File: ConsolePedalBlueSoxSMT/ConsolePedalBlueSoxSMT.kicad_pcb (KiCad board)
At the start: 2 copper layers, 100 x 60 mm, 53 parts, among them IC1 CD4013BE, J1 Conn_02x25_Counter_Clockwise, Q1 2N3904, Q2 2N3904, Q3 2N3904, U1 RC4558

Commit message: Minor changes
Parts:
- moved C100 76.4 mm to (174.2, 79.8), turned to 270 degrees
- moved C4 65.5 mm to (104.6, 81.8), turned to 270 degrees
- moved C101 58.9 mm to (160.0, 105.2), turned to 270 degrees
- moved C8 55.1 mm to (124.5, 96.0), turned to 90 degrees
- moved R102 51.2 mm to (135.2, 89.9), turned to 180 degrees
- moved C9 49.1 mm to (120.9, 96.0)
- moved R16 46.7 mm to (124.5, 101.6), turned to 90 degrees
- moved C2 41.0 mm to (127.0, 85.3), turned to 90 degrees
- moved R5 40.4 mm to (115.2, 72.6), turned to 0 degrees
- moved C102 32.3 mm to (138.7, 104.1), turned to 270 degrees
- moved R6 29.5 mm to (132.8, 85.9), turned to 180 degrees
- moved R101 28.6 mm to (130.2, 89.9), turned to 180 degrees
- moved R9 21.0 mm to (106.2, 90.9), turned to 180 degrees
- moved R13 19.8 mm to (160.0, 96.3)
- moved R15 18.5 mm to (156.0, 96.3)
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
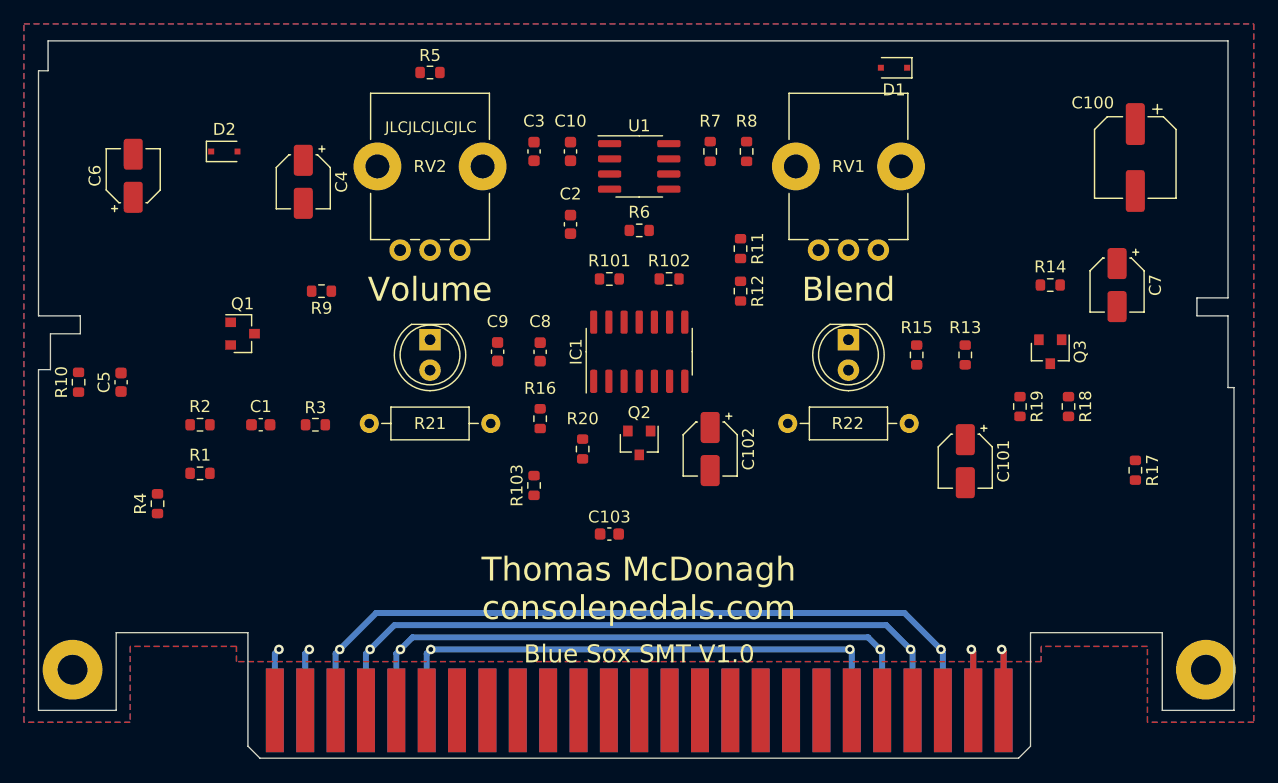
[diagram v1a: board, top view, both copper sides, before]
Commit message: Finished component placement
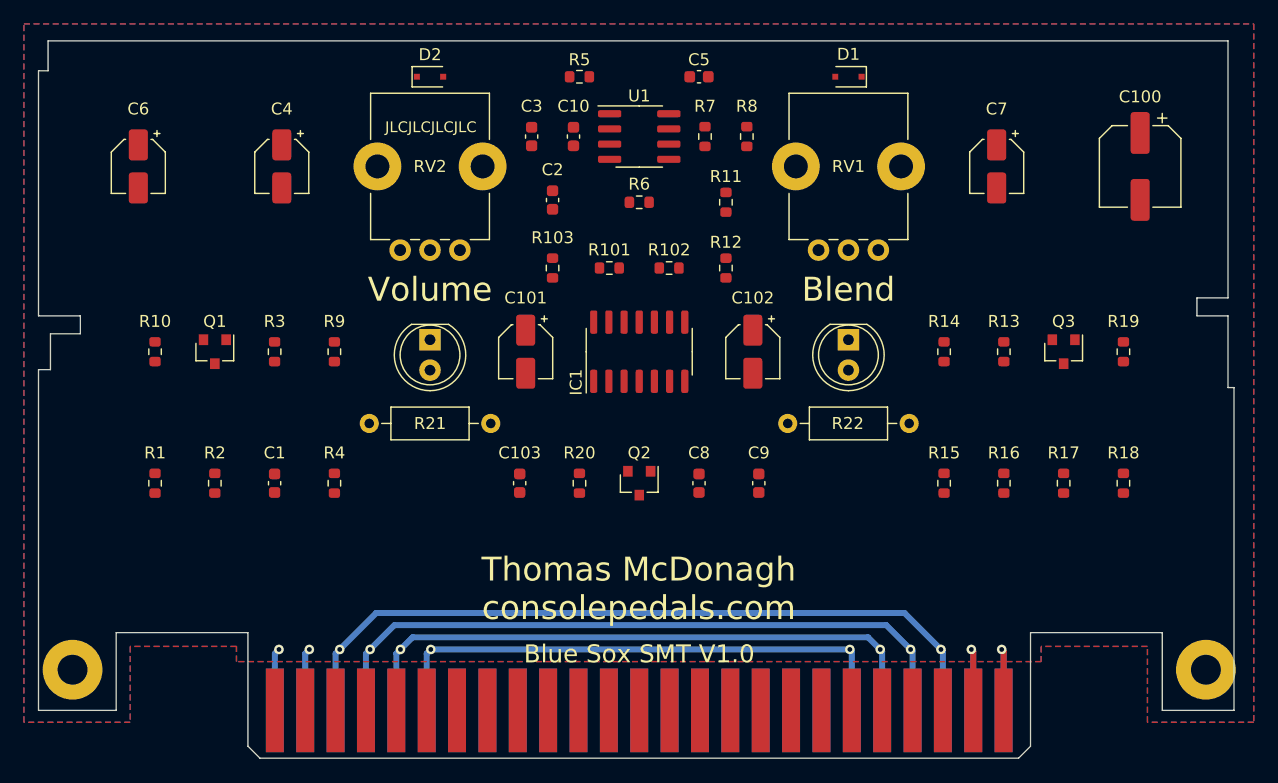
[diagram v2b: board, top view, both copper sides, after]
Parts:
- moved C5 54.7 mm to (137.8, 73.0), turned to 0 degrees
- moved R16 39.2 mm to (163.2, 107.0), turned to 270 degrees
- moved C101 37.9 mm to (123.2, 96.0)
- moved C9 24.5 mm to (142.8, 107.0)
- moved D2 18.3 mm to (115.2, 73.0)
- moved R103 18.3 mm to (125.5, 89.0)
- moved C8 17.2 mm to (137.8, 107.0)
- moved R4 14.9 mm to (107.2, 107.0), turned to 270 degrees
- moved C7 14.1 mm to (162.7, 80.5)
- moved R5 12.5 mm to (127.8, 73.0)
- moved R15 11.0 mm to (158.2, 107.0), turned to 90 degrees
- moved R14 10.5 mm to (158.2, 96.0), turned to 270 degrees
- moved R19 9.80 mm to (173.2, 96.0), turned to 90 degrees
- moved C102 8.89 mm to (142.2, 96.0)
- moved C103 8.62 mm to (122.8, 107.0), turned to 90 degrees
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
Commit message: Half of tracks laid out
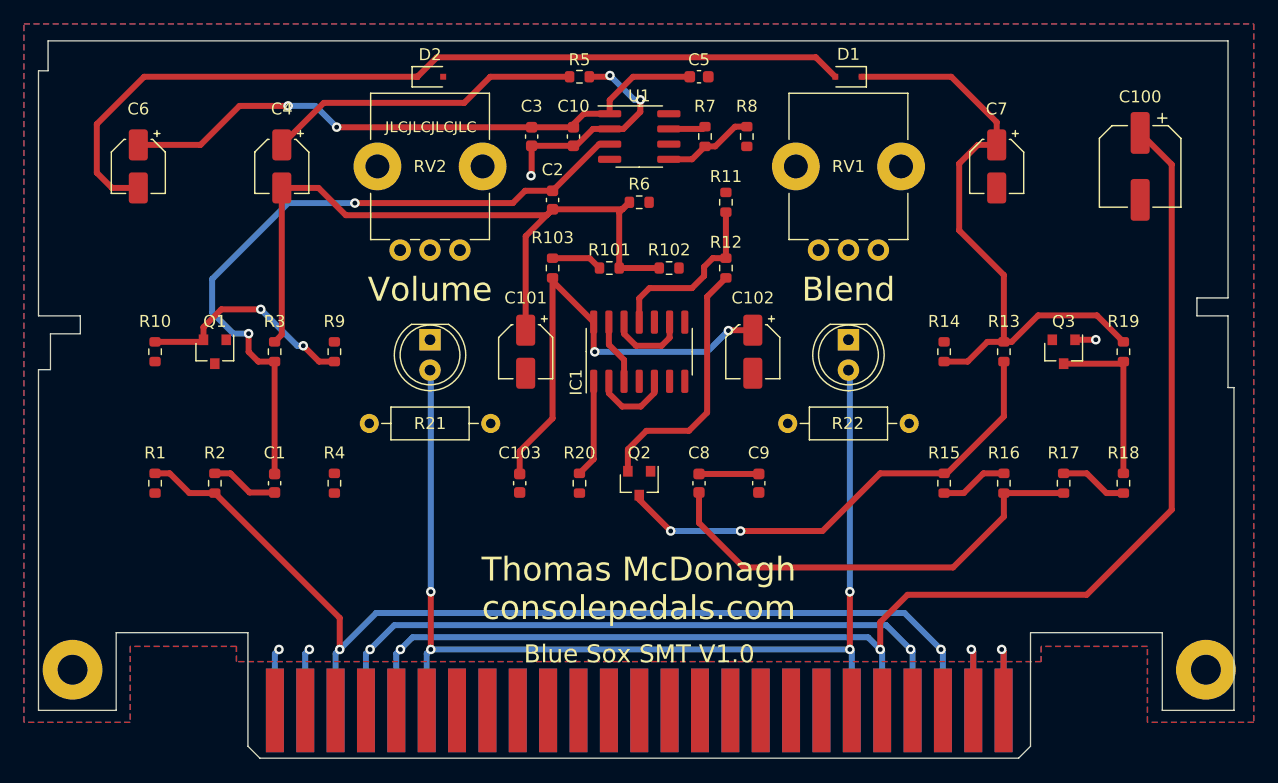
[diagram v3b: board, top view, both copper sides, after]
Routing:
- net Net-(C6-Pad2): track 0.00 -> 72.8 mm
- net +9V: track 51.4 -> 118.8 mm
- net /VREF: track 0.00 -> 63.8 mm
- net Net-(C1-Pad1): track 0.00 -> 57.9 mm, vias 0 -> 2
- net Net-(C7-Pad1): track 0.00 -> 52.5 mm
- net Net-(C10-Pad2): track 0.00 -> 50.8 mm, vias 0 -> 2
- net /LEDPower: track 45.5 -> 92.5 mm, vias 2 -> 4
- net Net-(Q2-Pad3): track 0.00 -> 40.5 mm, vias 0 -> 2
- net VDD: track 0.00 -> 39.2 mm, vias 0 -> 2
- net Net-(C8-Pad1): track 0.00 -> 38.3 mm
- net Net-(C4-Pad1): track 0.00 -> 26.4 mm
- net /Input: track 63.2 -> 86.3 mm
- net Net-(Q2-Pad2): track 0.00 -> 21.7 mm
- net Net-(C10-Pad1): track 0.00 -> 19.0 mm, vias 0 -> 3
- net Net-(Q1-Pad2): track 0.00 -> 18.6 mm, vias 0 -> 2
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
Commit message: Finalized traces. Need to export assembly files
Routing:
- net +9V: track 118.8 -> 194.0 mm, vias 2 -> 6
- net /CLK2: track 14.9 -> 76.4 mm, vias 0 -> 2
- net Net-(C8-Pad2): track 5.00 -> 60.2 mm, vias 0 -> 1
- net Net-(Q3-Pad2): track 0.00 -> 50.7 mm, vias 0 -> 2
- net Net-(R17-Pad1): track 5.68 -> 53.9 mm, vias 0 -> 2
- net Net-(R7-Pad2): track 3.10 -> 50.2 mm, vias 0 -> 2
- net /Output: track 57.3 -> 103.2 mm, vias 2 -> 3
- net Net-(C10-Pad1): track 19.0 -> 60.7 mm, vias 3 -> 4
- net Net-(C10-Pad2): track 50.8 -> 85.0 mm, vias 2 -> 4
- net Net-(R15-Pad1): track 5.68 -> 38.1 mm, vias 0 -> 1
- net /VREF: track 63.8 -> 83.9 mm
- net Net-(C5-Pad2): track 0.00 -> 16.3 mm
- net GND: track 32.9 -> 48.6 mm, vias 5 -> 8
- net Net-(D3-Pad1): track 0.00 -> 11.0 mm
- net Net-(D4-Pad1): track 0.00 -> 10.8 mm
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
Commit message: Added more info to silkscreen
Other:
- board text added: "+"
- board text added: "-"

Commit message: Fixed incorrect footprint and exported everything again
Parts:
- C102: footprint Capacitor_SMD:CP_Elec_4x5.4 -> Capacitor_SMD:CP_Elec_6.3x5.3
- moved C102 53.7 mm to (90.8, 80.5)
- moved C6 53.7 mm to (142.2, 96.0)
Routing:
- net VDD: track 39.2 -> 78.6 mm
- net Net-(C10-Pad2): track 85.0 -> 95.9 mm
- net Net-(C6-Pad2): track 72.8 -> 66.6 mm, vias 0 -> 2
- net GND: track 48.6 -> 51.4 mm, vias 8 -> 9
